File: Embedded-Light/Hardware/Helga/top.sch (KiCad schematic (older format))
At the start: 53 parts

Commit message: Helga: schematics updated
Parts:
- removed C?: 10n, Capacitors_SMD:C_0805, symbol C
- removed C?: 100n, Capacitors_SMD:C_0805, symbol C
- removed P?: UART, Pin_Headers:Pin_Header_Straight_1x04, symbol CONN_01X04
- removed P?: BAT, Pin_Headers:Pin_Header_Straight_1x02, symbol CONN_01X02
- removed R? (x2): 1k, Resistors_SMD:R_0805, symbol R
- removed R? (x2): 10k, Resistors_SMD:R_0805, symbol R
- added D?: LED2, Resistors_SMD:R_1210, symbol LED
- added P?: UART, symbol CONN_01X04
- added R?: 10k, Resistors_SMD:R_0805, symbol R
- added R?: 330, Resistors_SMD:R_0805, symbol R
- added U?: stm32h743zit6, symbol stm32h743zit6
- added W?: MCO, symbol TEST_1P
- D?: value LD1 -> LED1
- D?: value LD2 -> LED0
- Y?: value 20MHz -> 25 MHz
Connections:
- net labels added: CPIN1, CPIN10, CPIN11, CPIN12, CPIN13, CPIN14, CPIN15, CPIN16, CPIN17, CPIN18, CPIN19, CPIN2, CPIN20, CPIN3, CPIN4, CPIN5, CPIN6, CPIN7, CPIN8, CPIN9, VDD, backlight
- net labels removed: +5V, pwm_ch2, spi_clk, spi_miso, spi_mosi, spi_ss, usb_pon
- wire segments 208 -> 173
- no-connect marks 75 -> 7
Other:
- note added: "TODO: add simple audio amp"
- note added: "TODO: check BOOT and PDR_ON"
- note added: "TODO: place DT024 sym"
- note added: "TODO: place new uSD sym"
- moved on the sheet: C?, D?, P?, Q?, R?, SW?, Y?

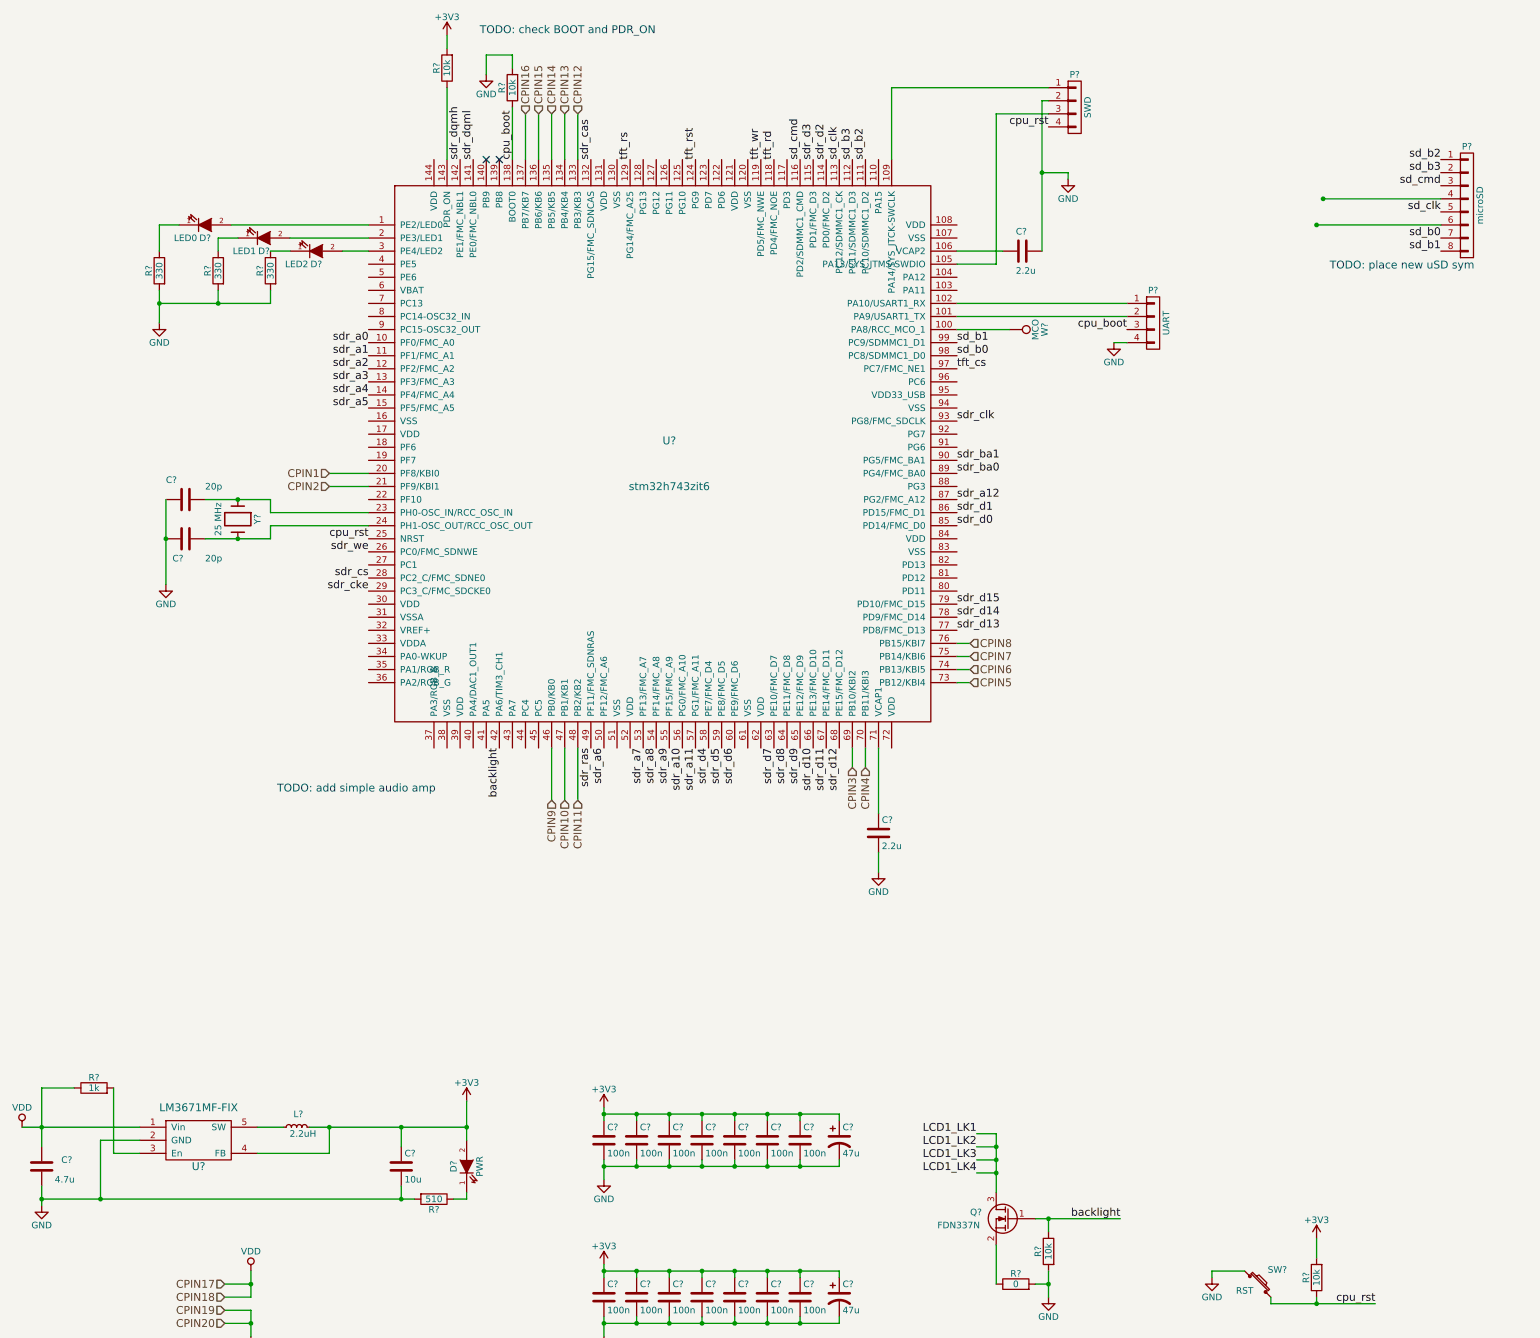
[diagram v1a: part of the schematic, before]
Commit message: Helga: added simple audio amplifier
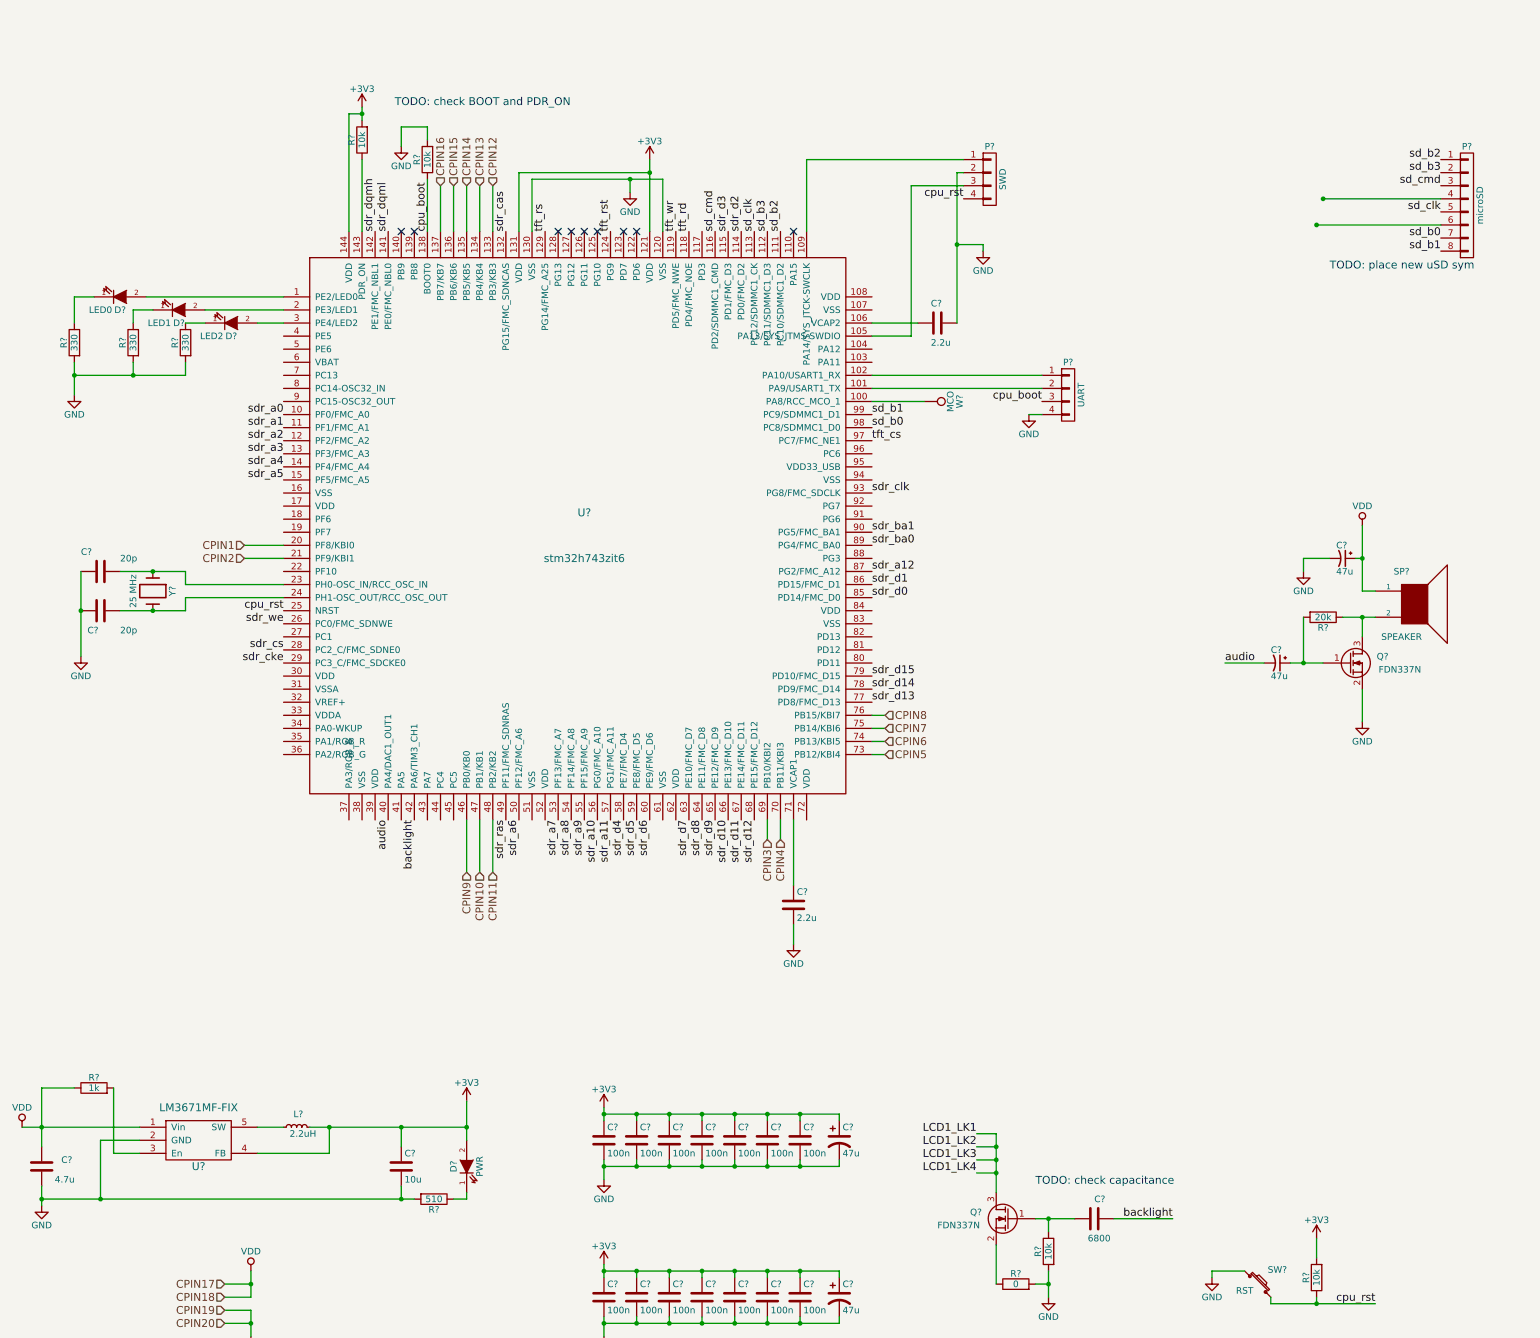
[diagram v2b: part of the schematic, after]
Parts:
- added C? (x2): 47u, symbol CP1_Small
- added C?: 6800, symbol C
- added Q?: FDN337N, TO_SOT_Packages_SMD:SOT-23, symbol Q_NMOS_GSD
- added R?: 20k, symbol R
- added SP?: SPEAKER, symbol SPEAKER
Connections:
- net labels added: audio
- wire segments 173 -> 194
- no-connect marks 7 -> 14
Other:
- note added: "TODO: check capacitance"
- note removed: "TODO: add simple audio amp"
- moved on the sheet: C?, D?, P?, R?, U?, W?, Y?

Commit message: Helga: updated
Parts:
- removed P?: UART, symbol CONN_01X04
- added P?: UART, symbol CONN_01X03
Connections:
- wire segments 194 -> 183
- no-connect marks 14 -> 9
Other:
- note added: "TODO: USB OTG (without ID)"
- note added: "TODO: add BOOT and RESET buttons"
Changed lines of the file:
@@
 Text Label 14850 7450 0    60   ~ 0
 LCD1_LK4
-NoConn ~ 13650 7350
-NoConn ~ 13650 7450
-NoConn ~ 13650 7550
-NoConn ~ 13650 7650
-$Comp
-L +3V3 #PWR?
-U 1 1 5C9C88C8
-P 13350 7600
-F 0 "#PWR?" H 13350 7450 50  0001 C CNN
-F 1 "+3V3" H 13350 7740 50  0000 C CNN
-F 2 "" H 13350 7600 50  0000 C CNN
-F 3 "" H 13350 7600 50  0000 C CNN
-	1    13350 7600
-	1    0    0    -1
-$EndComp
-$Comp
-L GND #PWR?
-U 1 1 5C9C88C9
-P 13100 7450
-F 0 "#PWR?" H 13100 7200 50  0001 C CNN
-F 1 "GND" H 13100 7300 50  0000 C CNN
-F 2 "" H 13100 7450 50  0000 C CNN
-F 3 "" H 13100 7450 50  0000 C CNN
-	1    13100 7450
-	1    0    0    -1
-$EndComp
 $Comp
 L R R?
@@
 Text Label 13650 8250 2    60   ~ 0
 tft_rs
-NoConn ~ 13650 7750
 $Comp
 L GND #PWR?
@@
 Wire Wire Line
 	1450 2750 1300 2750
-Connection ~ 10800 2200
-Wire Wire Line
-	11750 2200 10800 2200
-Connection ~ 10850 2000
-Wire Wire Line
-	11750 2000 10850 2000
 Wire Wire Line
 	13650 4000 13600 4000
@@
 Wire Wire Line
 	13650 3500 13600 3500
-Connection ~ 13300 6950
-Wire Wire Line
-	13300 5950 13300 6950
 Wire Wire Line
 	13650 3400 13600 3400
@@
 Wire Wire Line
 	13650 2700 13600 2700
-Wire Wire Line
-	13350 7750 12750 7750
 Connection ~ 13250 8450
 Wire Wire Line
@@
 Wire Wire Line
 	12750 8450 12850 8450
-Wire Wire Line
-	12750 7750 12750 8450
 Connection ~ 15550 7350
 Wire Wire Line
 	14850 7350 15550 7350
-Connection ~ 13100 7250
 Connection ~ 15100 7250
-Wire Wire Line
-	13100 6950 15100 6950
 Wire Wire Line
 	15100 7250 14850 7250
@@
 Wire Wire Line
 	15550 7100 15550 7850
-Connection ~ 13350 7850
-Wire Wire Line
-	13350 7950 13650 7950
-Connection ~ 13350 7750
-Wire Wire Line
-	13350 7600 13350 7950
-Wire Wire Line
-	13350 7850 13650 7850
-Wire Wire Line
-	13100 7250 13650 7250
-Wire Wire Line
-	13100 6950 13100 7450
 Connection ~ 1350 5150
 Connection ~ 1900 5150
@@
 Wire Wire Line
 	1350 5500 1350 4850
-Text Label 8700 3550 2    60   ~ 0
-cpu_boot
 $Comp
 L GND #PWR?
 U 1 1 5C9DD1C4
-P 8600 3650
-F 0 "#PWR?" H 8600 3400 50  0001 C CNN
-F 1 "GND" H 8600 3500 50  0000 C CNN
-F 2 "" H 8600 3650 50  0000 C CNN
-F 3 "" H 8600 3650 50  0000 C CNN
-	1    8600 3650
-	1    0    0    -1
-$EndComp
-$Comp
-L CONN_01X04 P?
-U 1 1 5C9DD239
-P 8900 3500
-F 0 "P?" H 8900 3750 50  0000 C CNN
-F 1 "UART" V 9000 3500 50  0000 C CNN
-F 2 "" H 8900 3500 50  0000 C CNN
-F 3 "" H 8900 3500 50  0000 C CNN
-	1    8900 3500
-	1    0    0    -1
-$EndComp
-Wire Wire Line
-	8700 3650 8600 3650
+P 8600 3550
+F 0 "#PWR?" H 8600 3300 50  0001 C CNN
+F 1 "GND" H 8600 3400 50  0000 C CNN
+F 2 "" H 8600 3550 50  0000 C CNN
+F 3 "" H 8600 3550 50  0000 C CNN
+	1    8600 3550
+	1    0    0    -1
+$EndComp
+Wire Wire Line
+	8700 3550 8600 3550
 Wire Wire Line
 	7400 3350 8700 3350
@@
 NoConn ~ 5000 2250
 NoConn ~ 6800 2250
+Text Notes 7500 3250 0    60   ~ 0
+TODO: USB OTG (without ID)
+Text Notes 8900 7350 0    60   ~ 0
+TODO: add BOOT and RESET buttons
+$Comp
+L CONN_01X03 P?
+U 1 1 5C9FDE87
+P 8900 3450
+F 0 "P?" H 8900 3650 50  0000 C CNN
+F 1 "UART" V 9000 3450 50  0000 C CNN
+F 2 "" H 8900 3450 50  0000 C CNN
+F 3 "" H 8900 3450 50  0000 C CNN
+	1    8900 3450
+	1    0    0    -1
+$EndComp
 $EndSCHEMATC
